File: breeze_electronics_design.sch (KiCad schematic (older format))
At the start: 0 parts

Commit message: Finish STM32F103T8U6TR connect
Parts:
- added U?: STM32F103T8U6TR, symbol STM32F103T8U6TR
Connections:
- net labels added: BAT_DET, BOOT0, BT_EN, CE, CSN, GND, HM_INT, I2C_SCL, I2C_SDA, MISO, MOSI, MP_INT, NRF_IRQ, OSC_IN, OSC_OUT, PA11, PA8, PB1, PB3, PWMA, PWMB, PWMC, PWMD, RST, RXD_BT, SCK, SWCLK, SWDIO, TXD_BT, VCC3.3
- wire segments 0 -> 38
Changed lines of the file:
@@
 Comment4 ""
 $EndDescr
+$Comp
+L STM32F103T8U6TR U?
+U 1 1 57B1D789
+P 3300 2600
+F 0 "U?" H 2650 3350 60  0000 C CNN
+F 1 "STM32F103T8U6TR" H 3300 2200 60  0000 C CNN
+F 2 "" H 3300 2700 60  0000 C CNN
+F 3 "" H 3300 2700 60  0000 C CNN
+	1    3300 2600
+	1    0    0    -1
+$EndComp
+Text Label 2000 2350 0    60   ~ 0
+OSC_IN
+Text Label 2000 2450 0    60   ~ 0
+OSC_OUT
+Text Label 2000 2550 0    60   ~ 0
+RST
+Text Label 2000 2650 0    60   ~ 0
+GND
+Text Label 2000 2850 0    60   ~ 0
+PWMA
+Text Label 2000 2950 0    60   ~ 0
+PWMB
+Text Label 2000 3050 0    60   ~ 0
+PWMC
+Text Label 1900 2050 0    60   ~ 0
+VCC3.3
+Text Label 2900 1450 1    60   ~ 0
+GND
+Text Label 3000 1550 1    60   ~ 0
+BOOT0
+Text Label 3100 1650 1    60   ~ 0
+I2C_SDA
+Text Label 3200 1650 1    60   ~ 0
+I2C_SCL
+Text Label 3300 1600 1    60   ~ 0
+MP_INT
+Text Label 3500 1450 1    60   ~ 0
+PB3
+Text Label 3600 1650 1    60   ~ 0
+NRF_IRQ
+Text Label 3700 1600 1    60   ~ 0
+SWCLK
+Text Label 3400 1600 1    60   ~ 0
+HM_INT
+Text Label 4350 2450 0    60   ~ 0
+SWDIO
+Text Label 4500 2550 0    60   ~ 0
+CE
+Text Label 4400 2650 0    60   ~ 0
+PA11
+Text Label 4300 2750 0    60   ~ 0
+RXD_BT
+Text Label 4300 2850 0    60   ~ 0
+TXD_BT
+Text Label 4450 2950 0    60   ~ 0
+PA8
+Text Label 4700 2050 2    60   ~ 0
+VCC3.3
+$Comp
+L GND #PWR?
+U 1 1 57B1E09C
+P 4750 2350
+F 0 "#PWR?" H 4750 2100 50  0001 C CNN
+F 1 "GND" H 4750 2200 50  0000 C CNN
+F 2 "" H 4750 2350 50  0000 C CNN
+F 3 "" H 4750 2350 50  0000 C CNN
+	1    4750 2350
+	0    -1   -1   0
+$EndComp
+Text Label 2900 3650 3    60   ~ 0
+PWMD
+Text Label 3000 3750 3    60   ~ 0
+CSN
+Text Label 3100 3750 3    60   ~ 0
+SCK
+Text Label 3200 3700 3    60   ~ 0
+MISO
+Text Label 3300 3700 3    60   ~ 0
+MOSI
+Text Label 3400 3550 3    60   ~ 0
+BAT_DET
+Text Label 3500 3750 3    60   ~ 0
+PB1
+Text Label 3600 3650 3    60   ~ 0
+BT_EN
+$Comp
+L GND #PWR?
+U 1 1 57B1E2A8
+P 3700 3800
+F 0 "#PWR?" H 3700 3550 50  0001 C CNN
+F 1 "GND" H 3700 3650 50  0000 C CNN
+F 2 "" H 3700 3800 50  0000 C CNN
+F 3 "" H 3700 3800 50  0000 C CNN
+	1    3700 3800
+	1    0    0    -1
+$EndComp
+Wire Wire Line
+	2000 3050 2400 3050
+Wire Wire Line
+	2400 2450 2000 2450
+Wire Wire Line
+	2400 2350 2000 2350
+Wire Wire Line
+	2000 2550 2400 2550
+Wire Wire Line
+	2000 2650 2400 2650
+Wire Wire Line
+	2000 2850 2400 2850
+Wire Wire Line
+	2000 2950 2400 2950
+Wire Wire Line
+	1900 2050 1900 2750
+Wire Wire Line
+	1900 2750 2400 2750
+Wire Wire Line
+	2400 2250 1900 2250
+Connection ~ 1900 2250
+Wire Wire Line
+	2900 1300 2900 1700
+Wire Wire Line
+	3000 1300 3000 1700
+Wire Wire Line
+	3100 1300 3100 1700
+Wire Wire Line
+	3200 1300 3200 1700
+Wire Wire Line
+	3300 1300 3300 1700
+Wire Wire Line
+	3400 1300 3400 1700
+Wire Wire Line
+	3500 1300 3500 1700
+Wire Wire Line
+	3600 1300 3600 1700
+Wire Wire Line
+	3700 1300 3700 1700
+Wire Wire Line
+	4600 2450 4200 2450
+Wire Wire Line
+	4200 2550 4600 2550
+Wire Wire Line
+	4200 2650 4600 2650
+Wire Wire Line
+	4200 2750 4600 2750
+Wire Wire Line
+	4200 2850 4600 2850
+Wire Wire Line
+	4200 2950 4600 2950
+Wire Wire Line
+	4200 3050 4700 3050
+Wire Wire Line
+	4700 3050 4700 2050
+Wire Wire Line
+	4200 2250 4700 2250
+Connection ~ 4700 2250
+Wire Wire Line
+	4200 2350 4750 2350
+Wire Wire Line
+	2900 3500 2900 3900
+Wire Wire Line
+	3000 3500 3000 3900
+Wire Wire Line
+	3100 3500 3100 3900
+Wire Wire Line
+	3200 3500 3200 3900
+Wire Wire Line
+	3300 3500 3300 3900
+Wire Wire Line
+	3400 3500 3400 3900
+Wire Wire Line
+	3500 3500 3500 3900
+Wire Wire Line
+	3600 3500 3600 3900
+Wire Wire Line
+	3700 3500 3700 3800
 $EndSCHEMATC

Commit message: Finish the basic schematic
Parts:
- added A?: Antenna, symbol Antenna
- added C? (x9): 0.1UF, symbol Capacitance
- added C? (x12): 2.2UF, symbol Capacitance
- added C? (x2): 22PF, symbol Capacitance
- added C? (x2): 2.2NF, symbol Capacitance
- added C?: 4.7PF, symbol Capacitance
- added C?: 1.5PF, symbol Capacitance
- added C?: 1PF, symbol Capacitance
- added C?: 220NF, symbol Capacitance
- added C?: 4.7UF, symbol Capacitance
- added C? (x2): 10UF, symbol CapacitancePolar
- added C?: 220PF, symbol Capacitance
- added D?: M1_LED_TOP, symbol Led
- added D?: M1_LED_BOT, symbol Led
- added D? (x2): MBR0520, symbol SchottkyDiode
- added D?: M2_LED_TOP, symbol Led
- added D?: M2_LED_BOT, symbol Led
- added D?: M3_LED_TOP, symbol Led
- added D?: M3_LED_BOT, symbol Led
- added D?: M4_LED_TOP, symbol Led
- added D?: M4_LED_BOT, symbol Led
- added H?: Header, symbol Header
- added J?: SIP4, symbol SIP4
- added L?: 2.7NH, symbol Inductor
- added L?: 8.2NH, symbol Inductor
- added L?: 3.9NH, symbol Inductor
- added L?: 4.7UH, symbol Inductor
- added LED?: POWER, symbol Led
- added LED?: BT_LED, symbol Led
- added LED?: CHG_LED, symbol Led
- added M? (x4): Motor, symbol Motor
- added Q?: S8050, symbol Triode
- added Q? (x4): SI2303, SOT-23, symbol Mosfet
- added R? (x4): 10K, symbol Resistor
- added R? (x6): 100, symbol Resistor
- added R?: 22K, symbol Resistor
- added R? (x7): 33K, symbol Resistor
- added R? (x4): 3K, symbol Resistor
- added R?: 1.65K, symbol Resistor
- added S?: SW2X3, symbol SW2X3
- added U?: CP2102, symbol CP2102
- added U?: NRF24L01, symbol NRF24L01
- added U?: HM-06-BT, symbol HM-06-BT
- added U?: MHC5883, symbol MHC5883
- added U?: MS5611, symbol MS5611
- added U?: MPU6050, symbol MPU6050
- added U? (x2): MIC5205-3.3, symbol MIC5205-3.3
- added U?: LM27313, symbol LM27313
- added U?: LTC4054, symbol LTC4054
- added USB?: MicroUSB, symbol MicroUSB
- added X?: XTAL, symbol XTAL
- added Y?: Crystal, symbol Crystal
- gave numbers to parts that had none: 1
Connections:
- net labels added: +3.3V, +3.7V, +5V, ANT1, ANT2, BT_LED, CHG_LED, DN, DP, ET_EN, Q_SCK, Q_SDA, S1, S3, SETC, VBAT, VBUS, VCC5.0
- wire segments 38 -> 387
- no-connect marks 0 -> 50

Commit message: Modify the schematic of controller
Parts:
- removed Y?: Crystal, symbol Crystal
- added Y?: 8MHZ, CSTCE8M00G55R0, symbol CrystalSMD
- C? (x3): footprint (none) -> C0402
- R?: footprint (none) -> R0402
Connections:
- wire segments 387 -> 389
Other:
- note added: "Controller"
- moved on the sheet: C?, J?, R?, U1

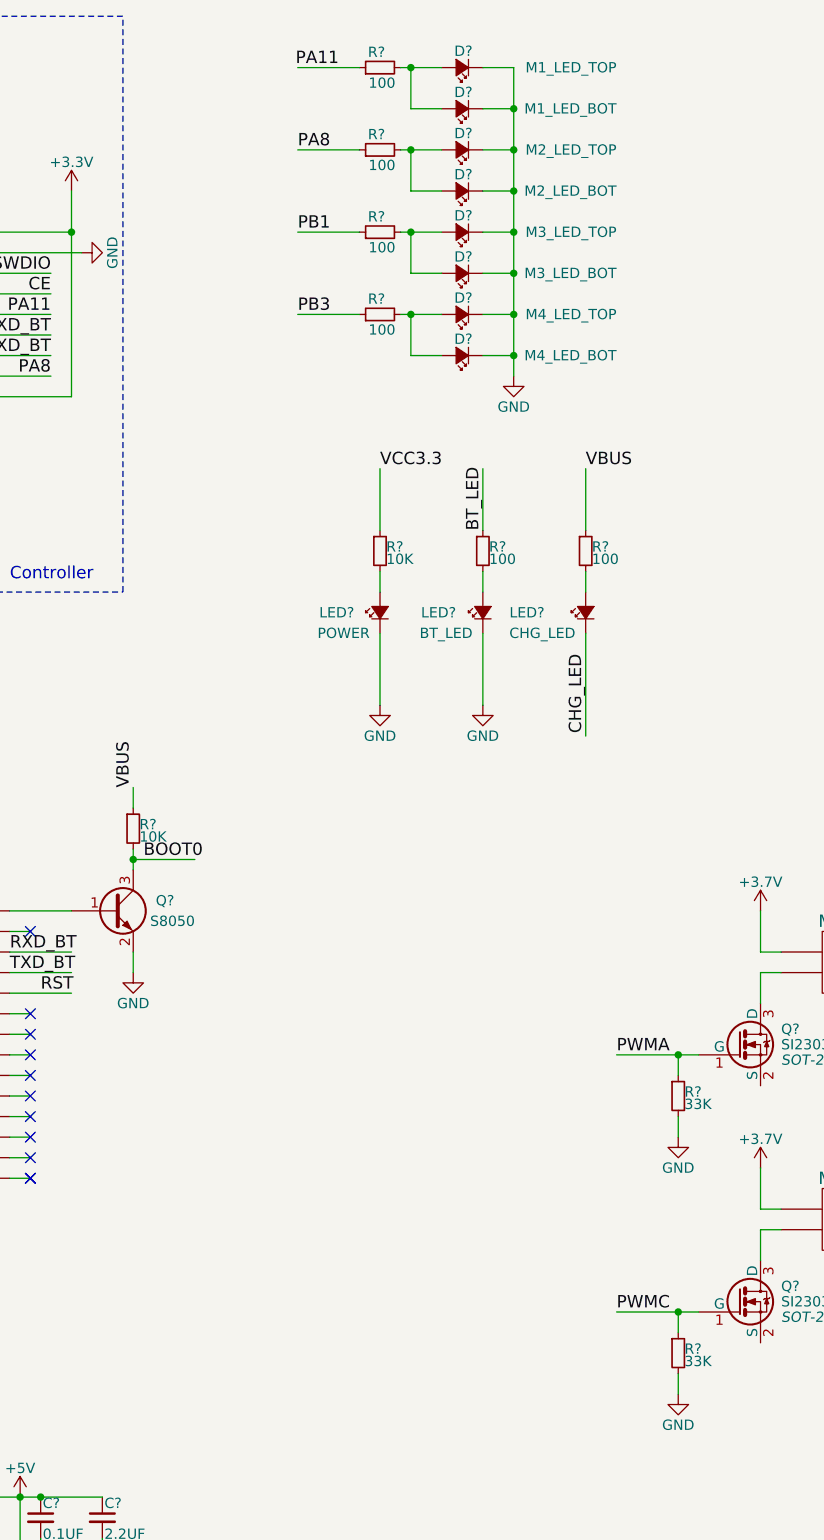
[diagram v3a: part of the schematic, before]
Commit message: Modify the schematic of leds
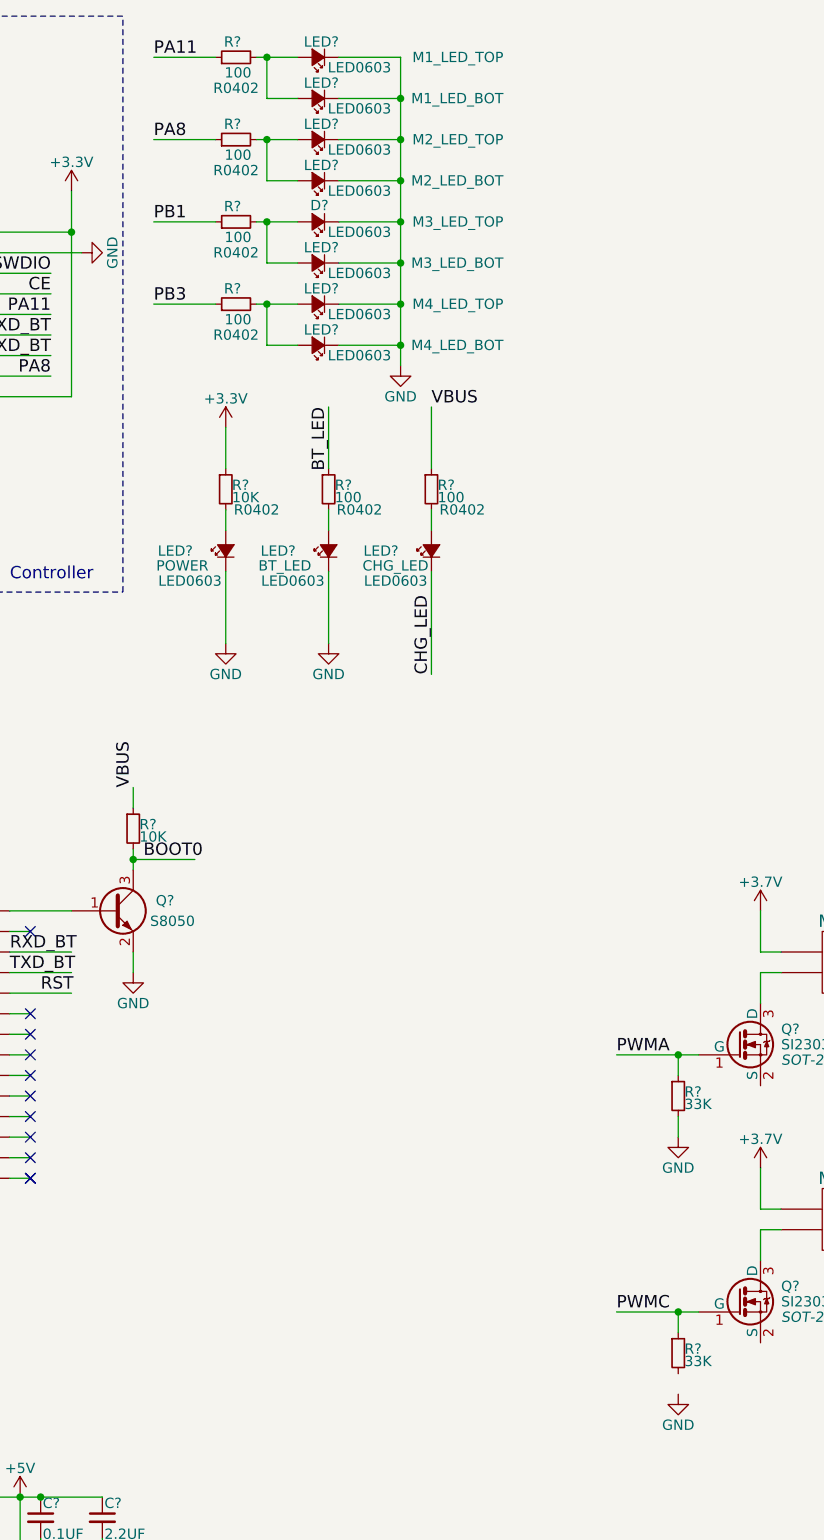
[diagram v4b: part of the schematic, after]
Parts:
- removed LED?: BT_LED, symbol Led
- removed LED?: CHG_LED, symbol Led
- added LED?: BT_LED, LED0603, symbol Led
- added LED?: CHG_LED, LED0603, symbol Led
- D?, LED?: footprint (none) -> LED0603
- LED? (x7): renamed from D?; footprint (none) -> LED0603
- R? (x7): footprint (none) -> R0402
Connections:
- wire segments 389 -> 388
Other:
- moved on the sheet: D?, LED?, R?

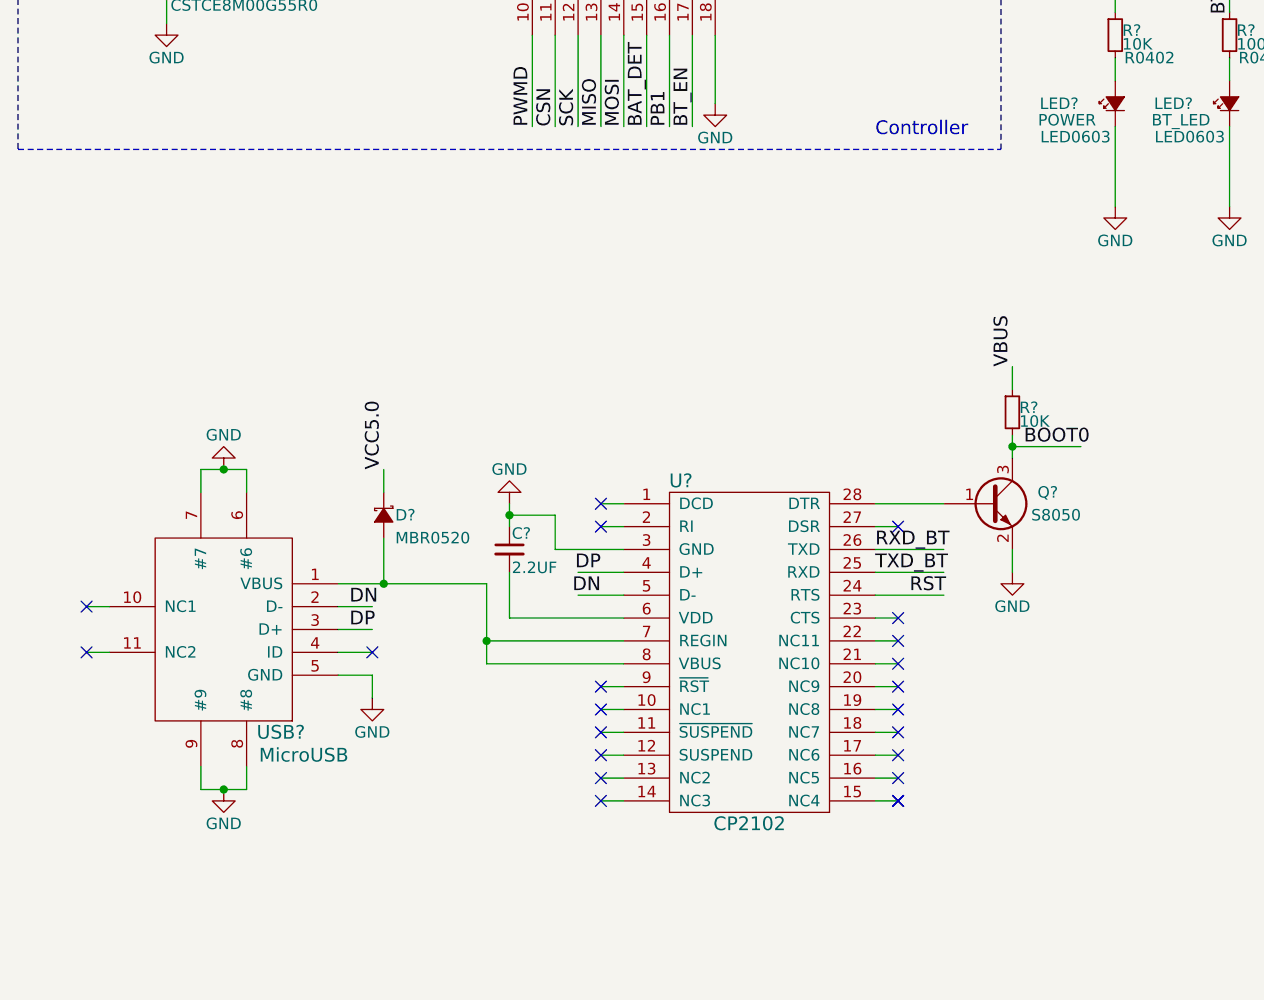
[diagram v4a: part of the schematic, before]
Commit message: Modify the schematic of usb_to_serial
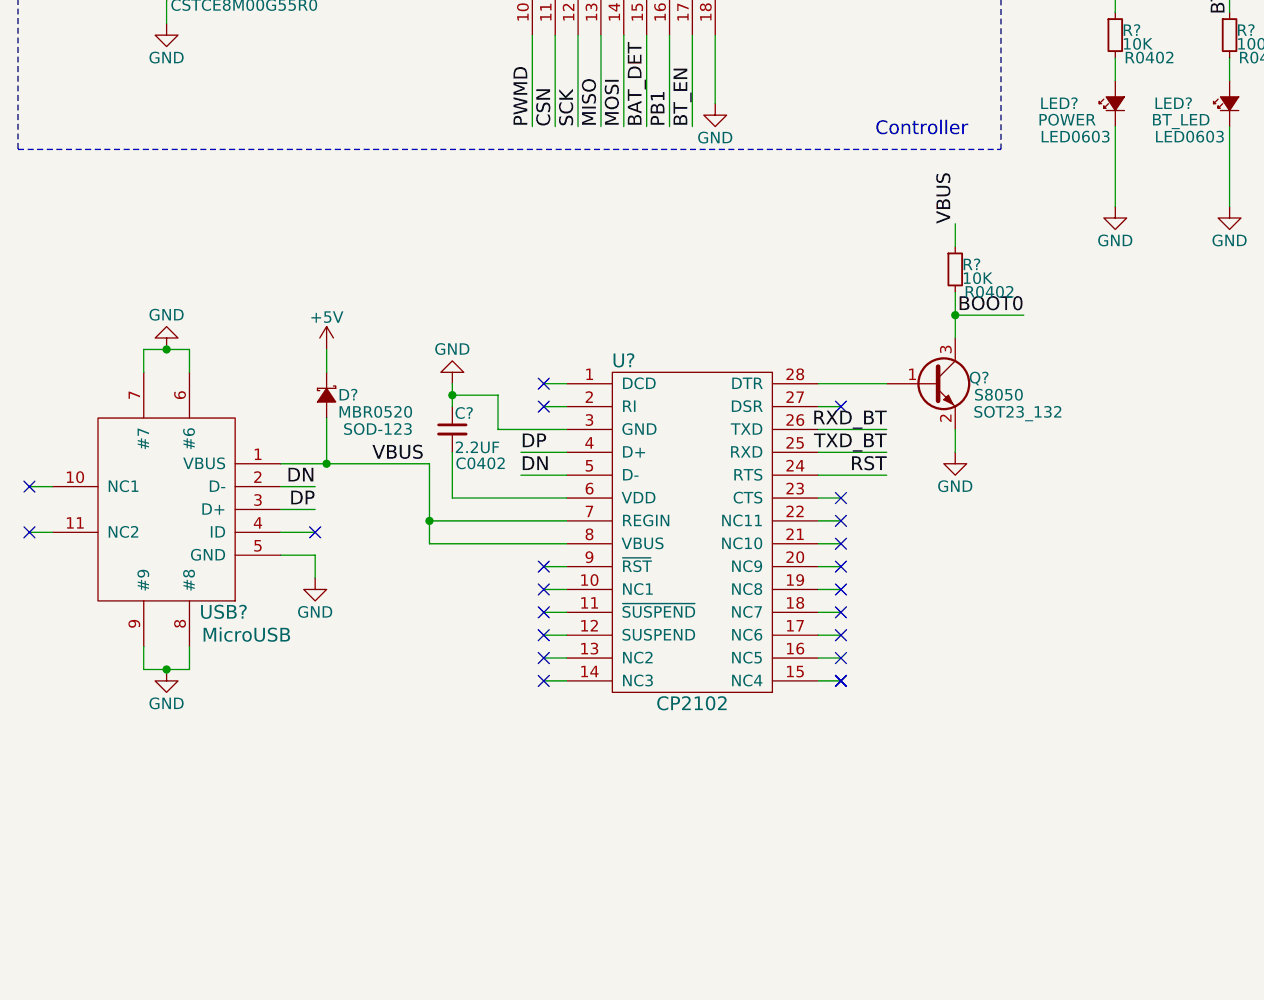
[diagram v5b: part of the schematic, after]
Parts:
- C?: footprint (none) -> C0402
- D?: footprint (none) -> SOD-123
- Q?: footprint (none) -> SOT23_132
- R?: footprint (none) -> R0402
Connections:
- net VCC5.0 is gone; now on net +5V: D?.1 (K)
- net VBUS: now also D?.2 (A), U?.7 (REGIN), U?.8 (VBUS), USB?.1 (VBUS)
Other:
- moved on the sheet: C?, D?, Q?, R?, U?, USB?
